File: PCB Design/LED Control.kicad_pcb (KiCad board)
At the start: 2 copper layers, 60 x 80 mm, 28 parts, among them J1 5V 5A Power, J2 TO WS2812B LED STRIP, J3 Sound Sensor, SW1 SW_Push_Dual

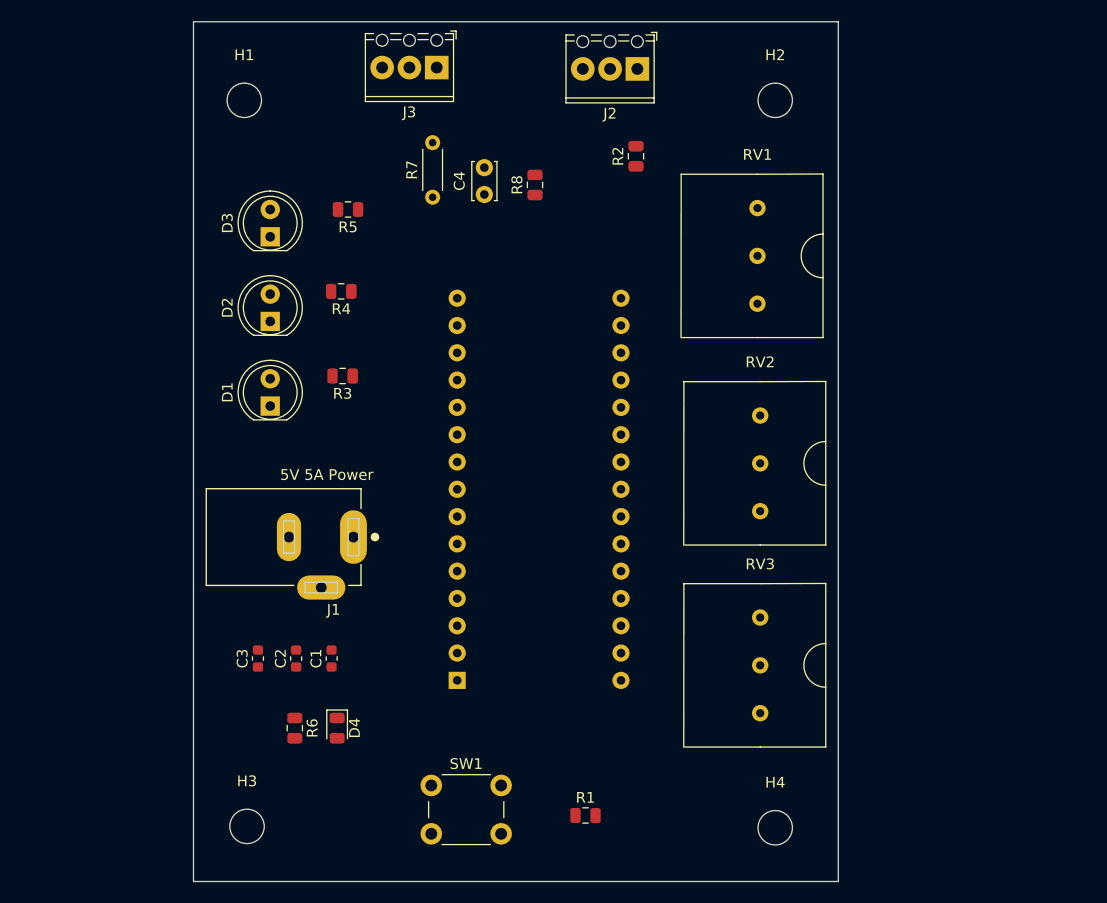
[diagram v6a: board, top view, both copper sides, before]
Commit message: power, gnd planes and traces
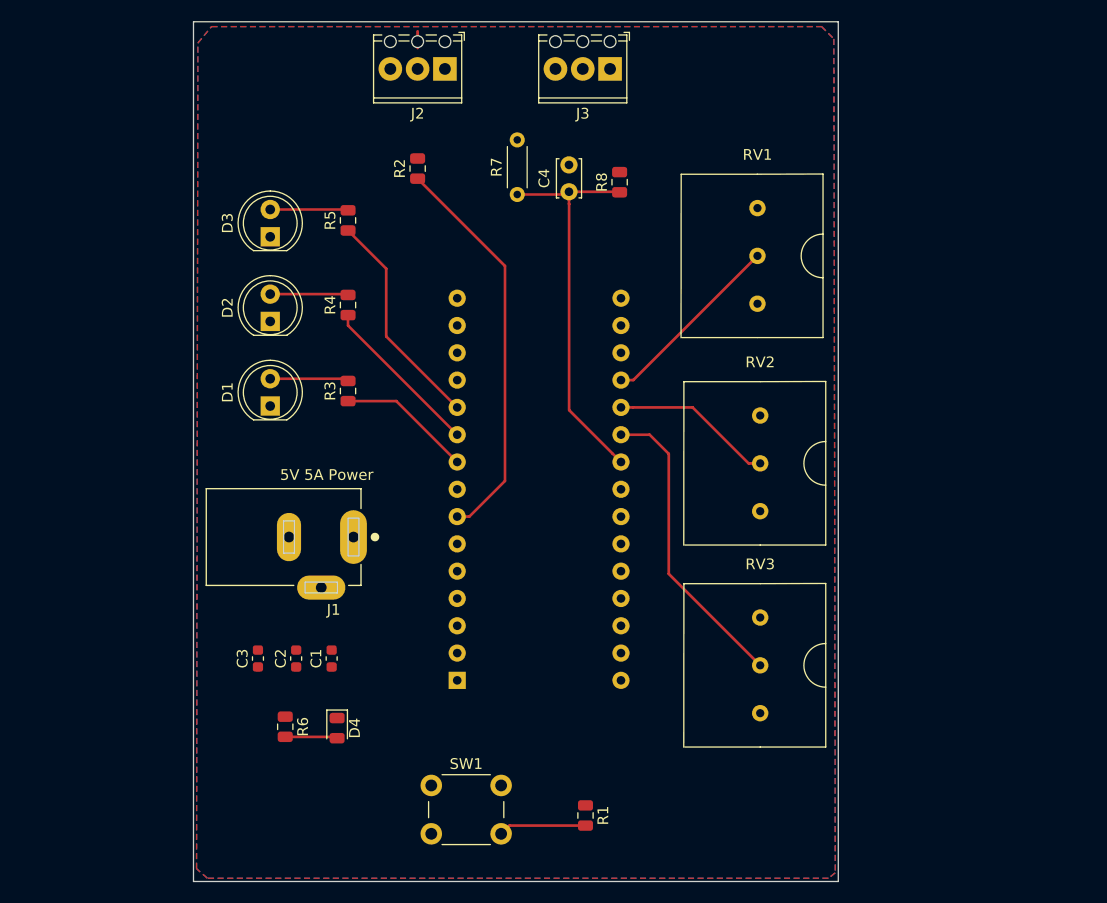
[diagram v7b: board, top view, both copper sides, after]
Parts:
- removed H1, H2, H3, H4: MountingHole_3.2mm_M3, MountingHole:MountingHole_3.2mm_M3
- moved R2 20.4 mm to (125.9, 73.7)
- moved J2 17.9 mm to (128.4, 64.4)
- moved J3 16.1 mm to (143.8, 64.4)
- moved C4 7.88 mm to (139.9, 75.8)
- moved R8 7.88 mm to (144.7, 74.9)
- moved R7 7.88 mm to (135.1, 76.1)
- moved R3 1.49 mm to (119.4, 94.4), turned to 90 degrees
- moved R4 1.42 mm to (119.4, 86.4), turned to 90 degrees
- moved R5 1.02 mm to (119.4, 78.5), turned to 90 degrees
- moved R6 0.90 mm to (113.5, 125.6)
- turned R1 to 270 degrees
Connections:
- A1 pad 22: Net-(A1-Pad22) -> A3
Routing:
- net Net-(A1-Pad7): track 0.00 -> 37.3 mm
- net A3: track 0.00 -> 36.8 mm
- net Net-(A1-Pad21): track 0.00 -> 28.4 mm
- net Net-(A1-Pad11): track 0.00 -> 20.7 mm
- net Net-(A1-Pad19): track 0.00 -> 17.5 mm
- net Net-(A1-Pad10): track 0.00 -> 15.3 mm
- net Net-(A1-Pad20): track 0.00 -> 15.1 mm
- net Net-(A1-Pad9): track 0.00 -> 12.5 mm
- net Net-(A1-Pad5): track 0.00 -> 8.17 mm
- net Net-(D1-Pad2): track 0.00 -> 7.68 mm
- net Net-(D3-Pad2): track 0.00 -> 7.27 mm
- net Net-(D2-Pad2): track 0.00 -> 7.27 mm
- net Net-(D4-Pad2): track 0.00 -> 4.88 mm
- net (no net): track 0.00 -> 1.56 mm
- added copper zone on B.Cu, net GND
- added copper zone on F.Cu, net VCC

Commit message: PCB completed
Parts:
- added PIN1: M3 HOLE, MountingHole:MountingHole_3.2mm_M3, F.Cu at (111.0, 66.0)
- added PIN3: M3 HOLE, MountingHole:MountingHole_3.2mm_M3, F.Cu at (159.0, 134.0)
- added PIN4: M3 HOLE, MountingHole:MountingHole_3.2mm_M3, F.Cu at (159.0, 66.0)
- added PIN4: M3 HOLE, MountingHole:MountingHole_3.2mm_M3, F.Cu at (111.0, 134.0)
- SW1: footprint Button_Switch_THT:SW_PUSH_6mm_H13mm -> Custom Footprint:Push_Button_Switch
- moved R1 13.9 mm to (128.0, 130.5), turned to 90 degrees
- moved SW1 13.6 mm to (140.7, 132.1), turned to 270 degrees
- moved C1 1.34 mm to (118.6, 118.1)
- moved C2 1.34 mm to (115.3, 118.1)
- moved C3 1.34 mm to (111.7, 118.1)
- moved R6 0.71 mm to (114.2, 125.7)
- moved D4 0.71 mm to (119.1, 125.9)
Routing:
- net Net-(A1-Pad27): track 0.00 -> 61.7 mm
- net GND: track 0.00 -> 27.1 mm, vias 0 -> 1
- net Net-(A1-Pad5): track 8.17 -> 30.0 mm
- net /SS_DATA_OUT: track 0.00 -> 10.3 mm
- net /DATA_IN: track 0.00 -> 8.33 mm
- net (no net): track 1.56 -> 0.00 mm
